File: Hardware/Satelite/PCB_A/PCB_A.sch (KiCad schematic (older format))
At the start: 29 parts, among them J1 Batería LiPo (Soldada), J2 CONUFL001-SMD, J3 Servo Globo, J4 Conector_PCB_A-B, J5 Servo Paracaídas, M1 Spacer, M2 Spacer, M3 Spacer, Q1 SSM3J338R,LF, Q2 BC817

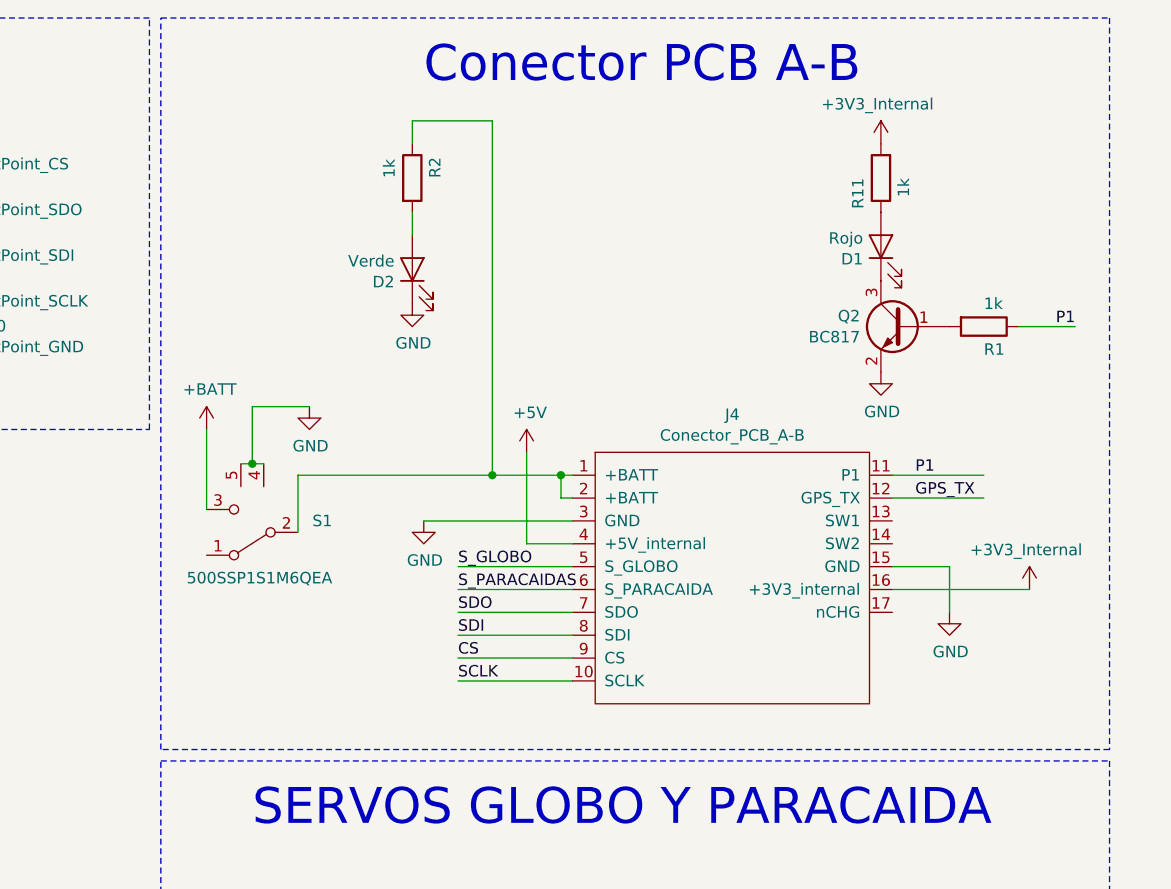
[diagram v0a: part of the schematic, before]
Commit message: Arreglos en PCB_A y PCB_B:
- El CI cargador de batería ya no alimenta al sistema, al conectar un cargador el mismo alimenta a la batería y al sistema de manera simultánea
- Ya no es necesario encender el CanSat para cargar la batería
- El interruptor del PCB_A ahora apaga todo el sistema independientemente si se está cargando o no la batería
- Agregado LED indicador de carga de batería
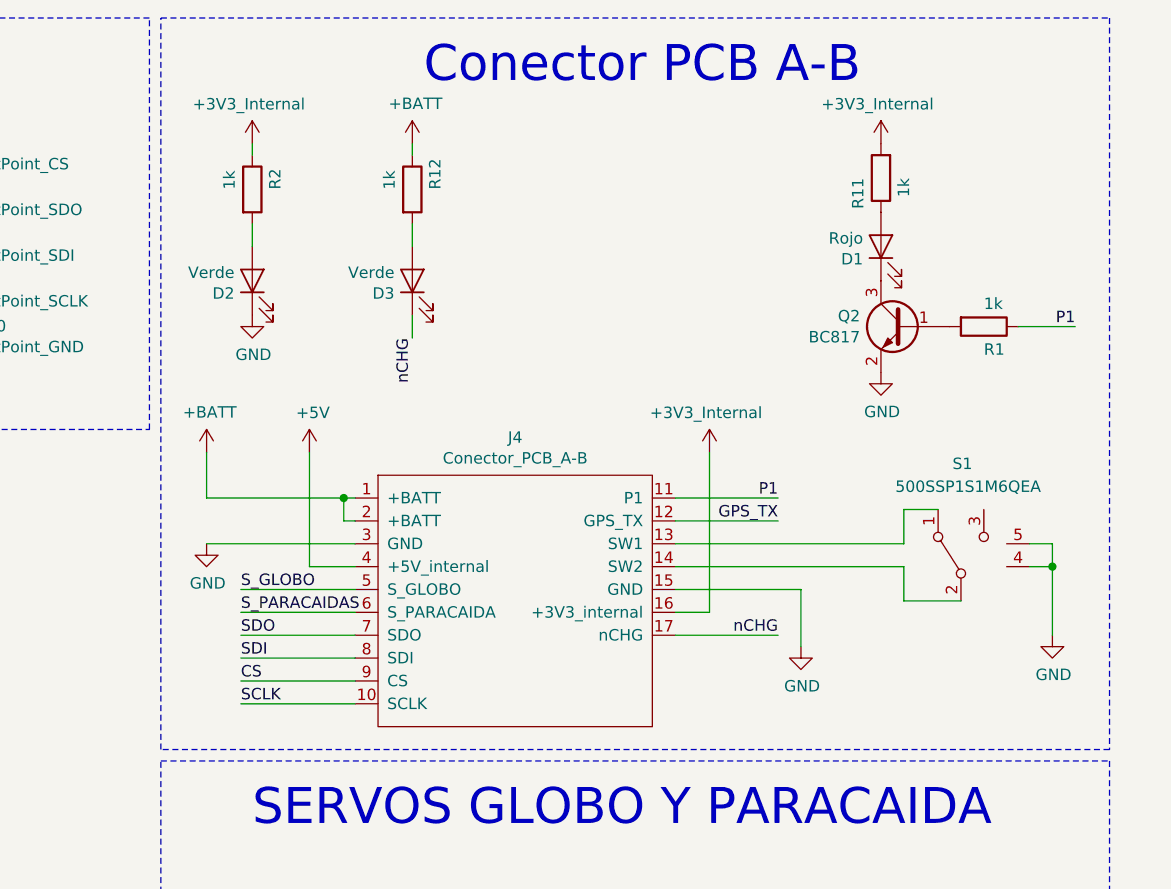
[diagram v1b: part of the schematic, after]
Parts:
- added D3: Verde, LED_SMD:LED_0603_1608Metric_Pad1.05x0.95mm_HandSolder, symbol Device:LED
- added R12: 1k, Resistor_SMD:R_0603_1608Metric_Pad1.05x0.95mm_HandSolder, symbol Device:R
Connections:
- net labels added: nCHG
- wire segments 73 -> 80
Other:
- moved on the sheet: D2, J4, R2, S1

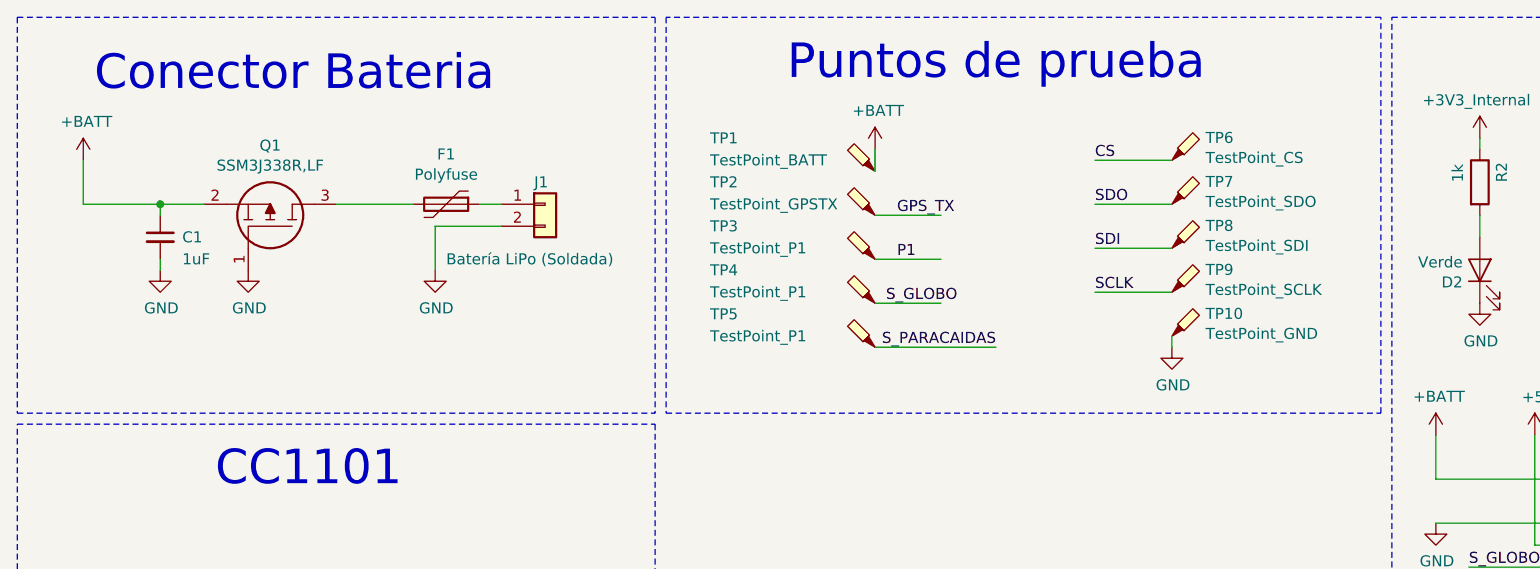
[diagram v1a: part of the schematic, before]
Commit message: Agregado circuito de protección para batería en PCB_A
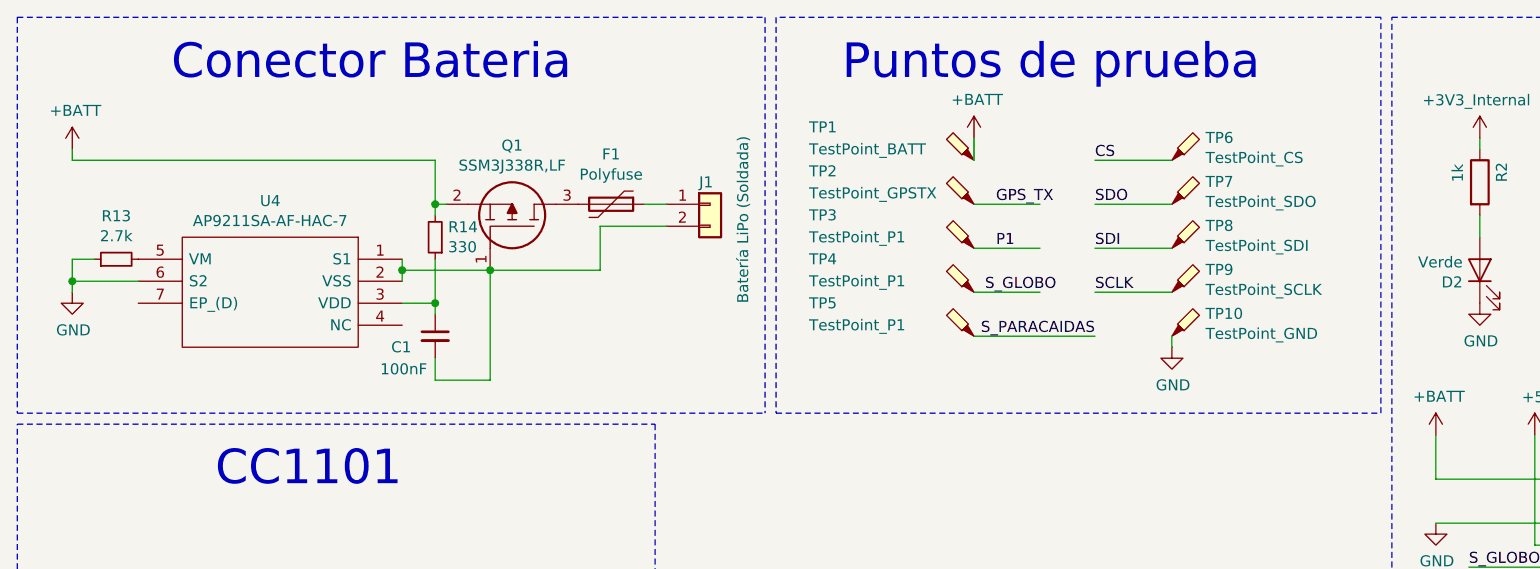
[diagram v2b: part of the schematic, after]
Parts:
- added R13: 2.7k, Resistor_SMD:R_0603_1608Metric_Pad1.05x0.95mm_HandSolder, symbol Device:R_Small
- added R14: 330, Resistor_SMD:R_0603_1608Metric_Pad1.05x0.95mm_HandSolder, symbol Device:R_Small
- added U4: AP9211SA-AF-HAC-7, AP9211SA-AF-HAC-7, symbol SamacSys_Parts:AP9211SA-AC-HAC-7
- C1: value 1uF -> 100nF; footprint Capacitor_SMD:C_0603_1608Metric_Pad1.05x0.95mm_HandSolder -> Capacitor_SMD:C_0402_1005Metric; Dielectric X7R -> (none); Manufacturer Part Number LMK107B7105MA-T -> GCM155R71C104KA55D; Voltage 10V -> (none)
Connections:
- wire segments 80 -> 93
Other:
- moved on the sheet: F1, J1, Q1, TP1, TP2, TP3, TP4, TP5

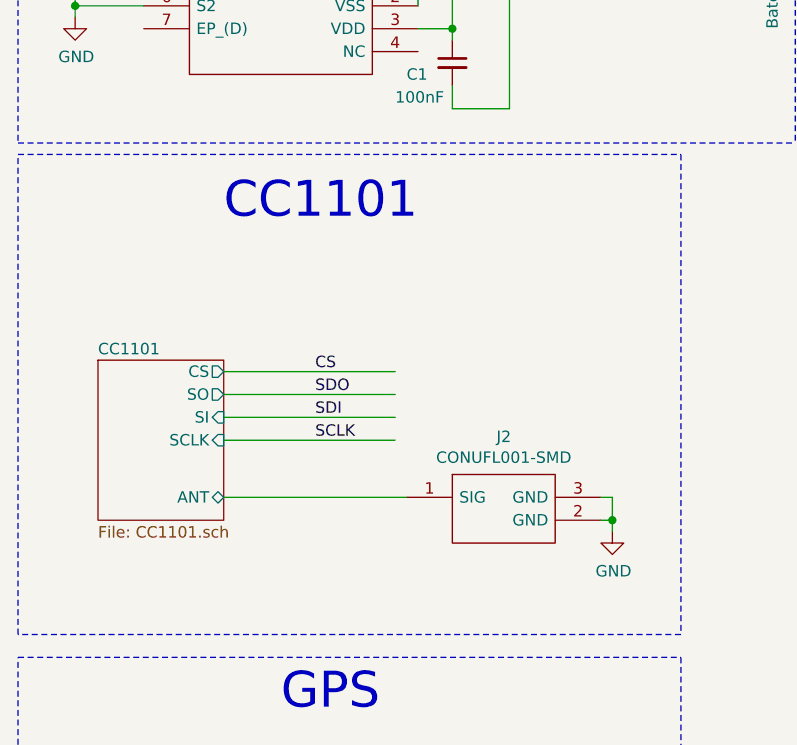
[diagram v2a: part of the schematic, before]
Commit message: Agregado extensor de rango CC1190 en PCB_A
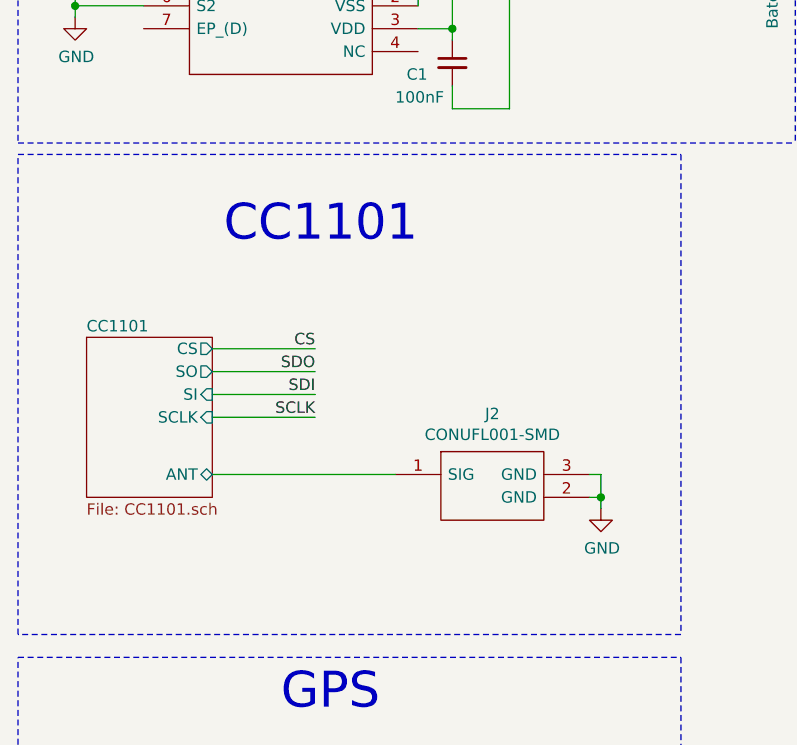
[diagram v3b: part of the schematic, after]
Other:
- moved on the sheet: J2
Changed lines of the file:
@@
 $EndSheet
 Wire Wire Line
-	1600 3450 2350 3450
-Wire Wire Line
-	1600 3550 2350 3550
-Wire Wire Line
-	1600 3650 2350 3650
+	1550 3350 2000 3350
+Wire Wire Line
+	1550 3450 2000 3450
+Wire Wire Line
+	1550 3550 2000 3550
 Wire Wire Line
 	1700 5450 2450 5450
-Text Label 2000 3450 0    50   ~ 0
+Text Label 2000 3350 2    50   ~ 0
 SDO
-Text Label 2000 3550 0    50   ~ 0
+Text Label 2000 3450 2    50   ~ 0
 SDI
-Text Label 2000 3650 0    50   ~ 0
+Text Label 2000 3550 2    50   ~ 0
 SCLK
 Text Label 2100 5450 0    50   ~ 0
@@
 GPS_TX
 $Sheet
-S 1050 3300 550  700
+S 1000 3200 550  700
 U 5BA17F9C
 F0 "CC1101" 50
 F1 "CC1101.sch" 50
-F2 "ANT" B R 1600 3900 50
-F3 "SCLK" I R 1600 3650 50
-F4 "SO" O R 1600 3450 50
-F5 "SI" I R 1600 3550 50
-F6 "CS" O R 1600 3350 50
+F2 "ANT" B R 1550 3800 50
+F3 "SCLK" I R 1550 3550 50
+F4 "SO" O R 1550 3350 50
+F5 "SI" I R 1550 3450 50
+F6 "CS" O R 1550 3250 50
 $EndSheet
 $Comp
@@
 CS
 Wire Wire Line
-	1600 3350 2350 3350
-Text Label 2000 3350 0    50   ~ 0
+	1550 3250 2000 3250
+Text Label 2000 3250 2    50   ~ 0
 CS
 $Comp
@@
 L power:GND #PWR06
 U 1 1 5BCC3FF5
-P 3300 4050
-F 0 "#PWR06" H 3300 3800 50  0001 C CNN
-F 1 "GND" H 3305 3877 50  0000 C CNN
-F 2 "" H 3300 4050 50  0001 C CNN
-F 3 "" H 3300 4050 50  0001 C CNN
-	1    3300 4050
-	1    0    0    -1
-$EndComp
-Wire Wire Line
-	2400 3900 1600 3900
+P 3250 3950
+F 0 "#PWR06" H 3250 3700 50  0001 C CNN
+F 1 "GND" H 3255 3777 50  0000 C CNN
+F 2 "" H 3250 3950 50  0001 C CNN
+F 3 "" H 3250 3950 50  0001 C CNN
+	1    3250 3950
+	1    0    0    -1
+$EndComp
+Wire Wire Line
+	2350 3800 1550 3800
 Text Notes 8100 850  0    157  ~ 0
 Conector PCB A-B\n
@@
 Wire Notes Line
 	700  4500 700  2400
-Text Notes 1600 2950 0    157  ~ 0
+Text Notes 1600 3050 0    157  ~ 0
 CC1101\n\n
 Text Notes 7350 4100 0    157  ~ 0
@@
 L SamacSys_Parts:CONUFL001-SMD J2
 U 1 1 5BC6411A
-P 2800 3900
-F 0 "J2" H 2825 4165 50  0000 C CNN
-F 1 "CONUFL001-SMD" H 2825 4074 50  0000 C CNN
-F 2 "SamacSys_Parts:CONUFL001-SMD" H 3100 4000 50  0001 L CNN
-F 3 "https://componentsearchengine.com/Datasheets/1/CONUFL001-SMD.pdf" H 3100 3900 50  0001 L CNN
-F 4 "RF Connectors / Coaxial Connectors U.FL Straight Surface Mount Jack" H 3100 3800 50  0001 L CNN "Description"
-F 5 "Linx Technologies" H 3100 3600 50  0001 L CNN "Manufacturer_Name"
-F 6 "CONUFL001-SMD" H 3100 3500 50  0001 L CNN "Manufacturer Part Number"
-F 7 "CONUFL001-SMD" H 3100 3200 50  0001 L CNN "Arrow Part Number"
-	1    2800 3900
-	1    0    0    -1
-$EndComp
-Wire Wire Line
-	3250 3900 3300 3900
-Wire Wire Line
-	3300 3900 3300 4000
-Wire Wire Line
-	3250 4000 3300 4000
-Connection ~ 3300 4000
-Wire Wire Line
-	3300 4000 3300 4050
+P 2750 3800
+F 0 "J2" H 2775 4065 50  0000 C CNN
+F 1 "CONUFL001-SMD" H 2775 3974 50  0000 C CNN
+F 2 "SamacSys_Parts:CONUFL001-SMD" H 3050 3900 50  0001 L CNN
+F 3 "https://componentsearchengine.com/Datasheets/1/CONUFL001-SMD.pdf" H 3050 3800 50  0001 L CNN
+F 4 "RF Connectors / Coaxial Connectors U.FL Straight Surface Mount Jack" H 3050 3700 50  0001 L CNN "Description"
+F 5 "Linx Technologies" H 3050 3500 50  0001 L CNN "Manufacturer_Name"
+F 6 "CONUFL001-SMD" H 3050 3400 50  0001 L CNN "Manufacturer Part Number"
+F 7 "CONUFL001-SMD" H 3050 3100 50  0001 L CNN "Arrow Part Number"
+	1    2750 3800
+	1    0    0    -1
+$EndComp
+Wire Wire Line
+	3200 3800 3250 3800
+Wire Wire Line
+	3250 3800 3250 3900
+Wire Wire Line
+	3200 3900 3250 3900
+Connection ~ 3250 3900
+Wire Wire Line
+	3250 3900 3250 3950
 Wire Wire Line
 	7300 3050 7800 3050

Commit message: Cambiado el nombre de la carpeta de liberías KiCad para no tener espacios ya que da problemas
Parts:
- U4: footprint AP9211SA-AF-HAC-7 -> SamacSys_Parts:AP9211SAACHAC7
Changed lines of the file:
@@
 F 0 "U4" H 3050 1915 50  0000 C CNN
 F 1 "AP9211SA-AF-HAC-7" H 3050 1824 50  0000 C CNN
-F 2 "AP9211SA-AF-HAC-7" H 3500 1750 50  0001 L CNN
+F 2 "SamacSys_Parts:AP9211SAACHAC7" H 3500 1750 50  0001 L CNN
 F 3 "https://www.diodes.com/assets/Datasheets/AP9211.pdf" H 3500 1650 50  0001 L CNN
 F 4 "Battery Management Multicell Batt MGR PMIC Protection Int" H 3500 1550 50  0001 L CNN "Description"
